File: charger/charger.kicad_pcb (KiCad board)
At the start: 2 copper layers, 42.7 x 32.5 mm, 13 parts, among them J1 USB4515-GF-A_REVA, J2 Screw_Terminal_2_P5.00mm

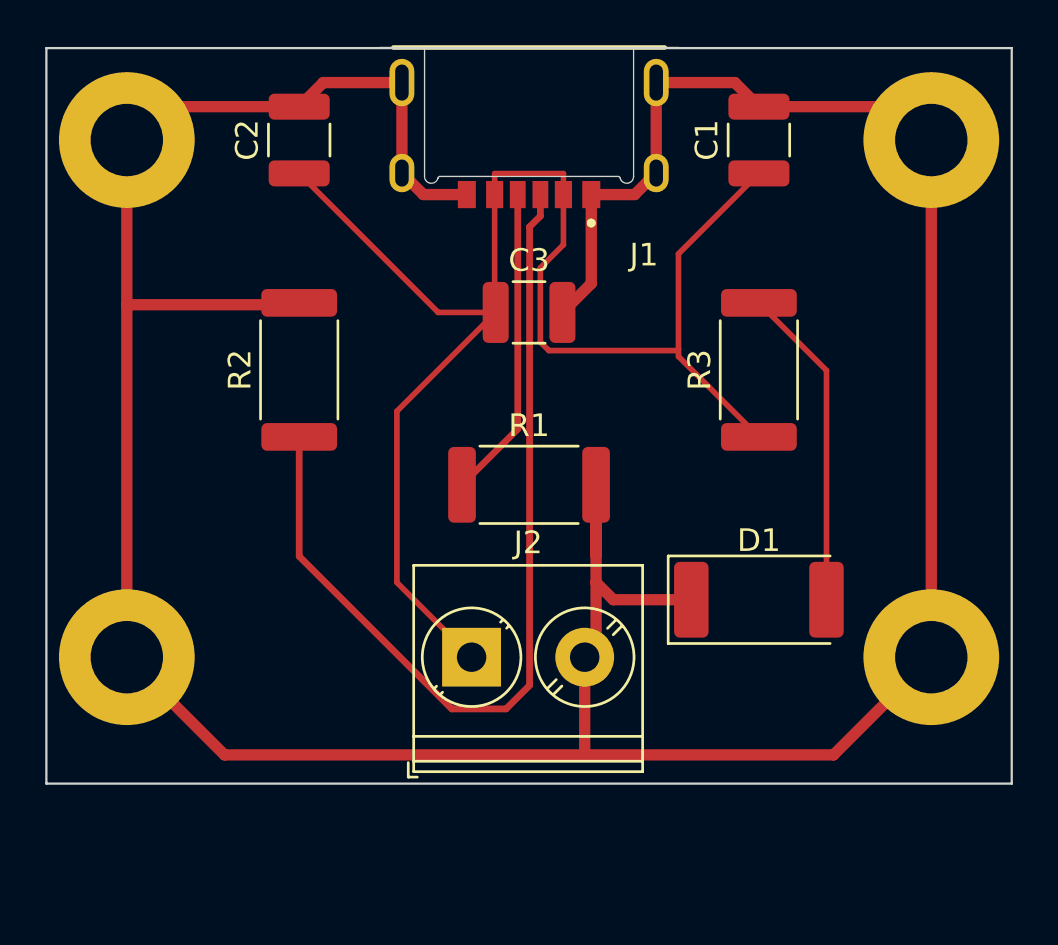
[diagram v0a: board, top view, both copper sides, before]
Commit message: added power/ground planes
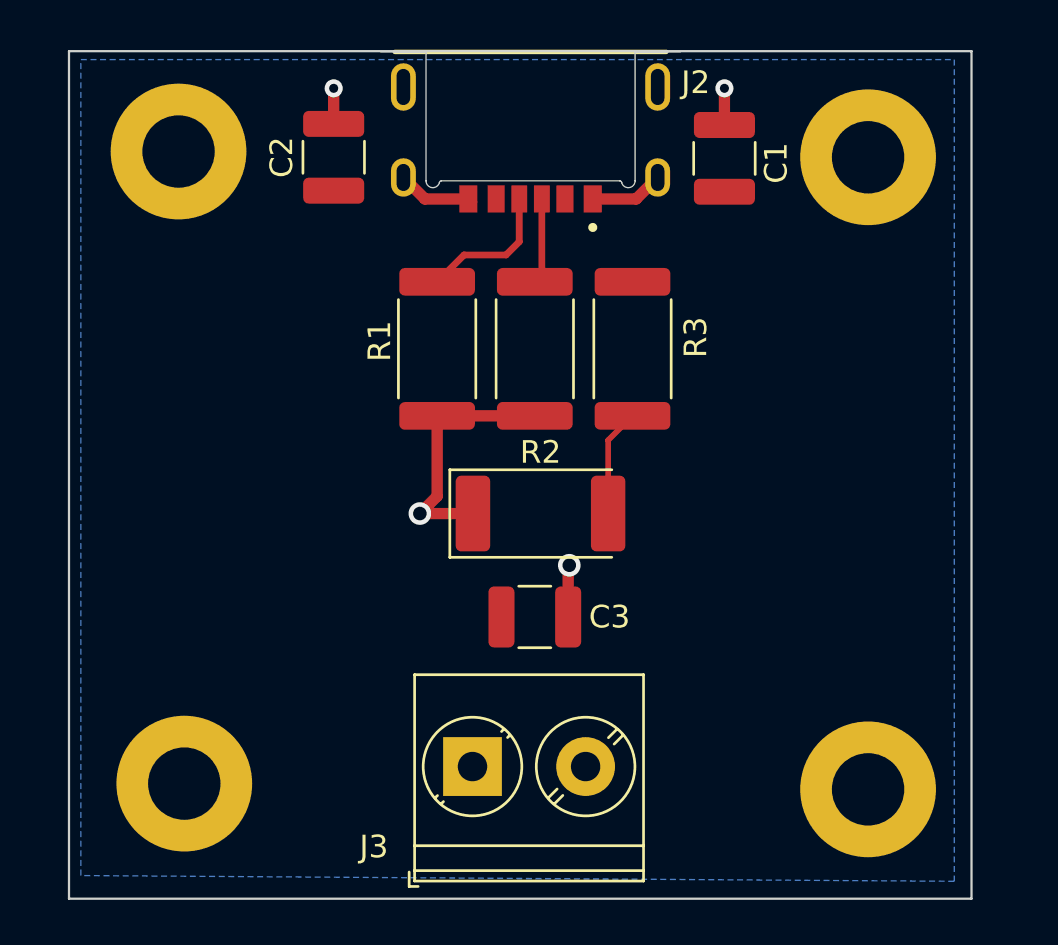
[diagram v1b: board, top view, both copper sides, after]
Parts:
- removed J1: USB4515-GF-A_REVA, USB4515-GF-A_REVA:GCT_USB4515-GF-A_REVA
- added J3: Screw_Terminal_2_P5.00mm, TerminalBlock_Phoenix:TerminalBlock_Phoenix_PT-1,5-2-5.0-H_1x02_P5.00mm_Horizontal, F.Cu at (99.1, 78.5)
- J2: value Screw_Terminal_2_P5.00mm -> USB4515-GF-A_REVA; footprint TerminalBlock_Phoenix:TerminalBlock_Phoenix_PT-1,5-2-5.0-H_1x02_P5.00mm_Horizontal -> USB4515-GF-A_REVA:GCT_USB4515-GF-A_REVA
- moved J2 25.3 mm to (101.7, 48.5), turned to 180 degrees
- moved C3 13.5 mm to (101.9, 71.9)
- moved R2 10.5 mm to (101.9, 60.0), turned to -90 degrees
- moved D1 10.4 mm to (102.1, 67.3)
- moved R1 7.26 mm to (97.5, 60.0), turned to -90 degrees
- moved H4 6.48 mm to (116.6, 79.5)
- moved H3 6.14 mm to (86.4, 79.2)
- moved R3 5.66 mm to (106.2, 60.0), turned to -90 degrees
- moved H2 2.90 mm to (116.6, 51.6)
- moved H1 2.34 mm to (86.1, 51.3)
- moved C1 1.73 mm to (110.2, 51.6)
- moved C2 1.70 mm to (93.0, 51.6)
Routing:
- net GND: track 159.0 -> 23.5 mm, vias 0 -> 4
- net +5V: track 67.6 -> 0.00 mm
- net /CC1: track 40.6 -> 3.79 mm
- net /LED: track 14.4 -> 4.76 mm
- net /CC2: track 13.9 -> 6.26 mm
- added copper zone on B.Cu, net GND
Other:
- board size 42.7 x 32.5 mm -> 39.9 x 37.5 mm

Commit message: fixed segments edge.cuts error and changed the pcb a little bit
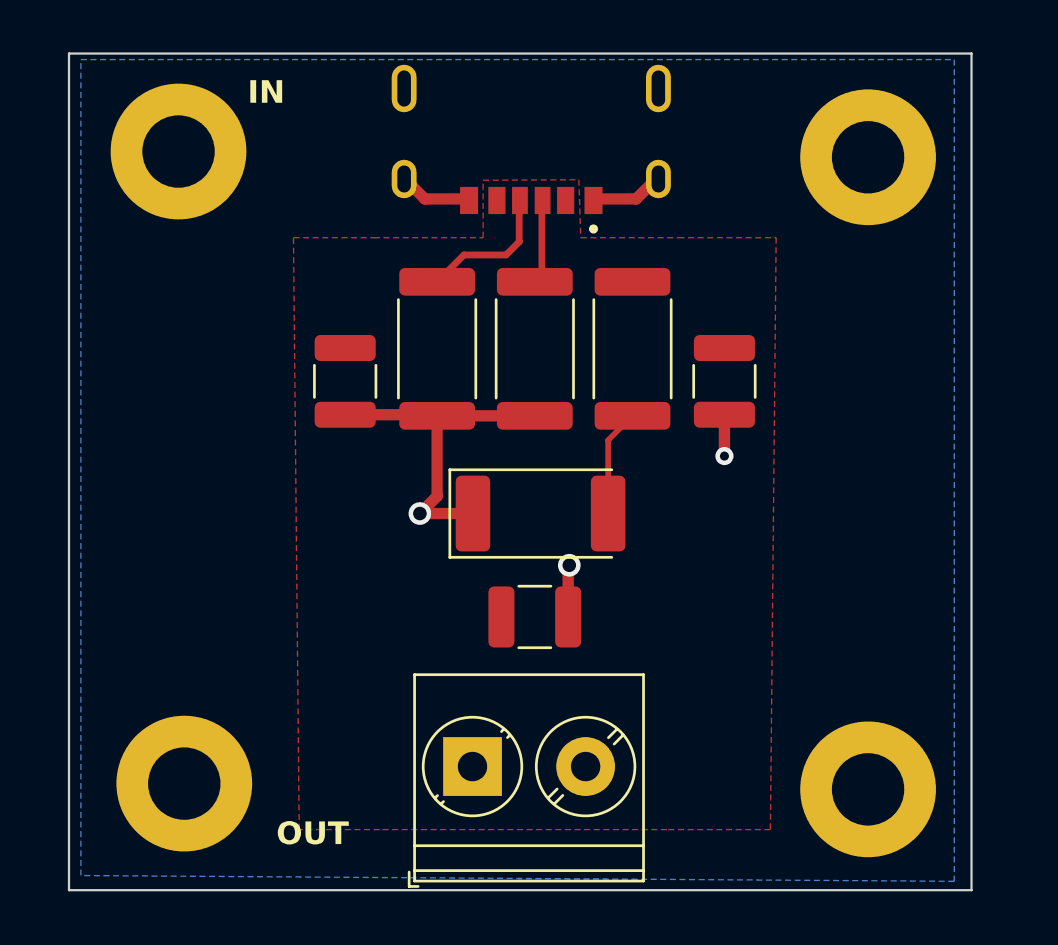
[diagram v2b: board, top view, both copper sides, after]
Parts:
- J2: footprint USB4515-GF-A_REVA:GCT_USB4515-GF-A_REVA -> connectors:USBC_PD_6PINS
- moved C2 9.92 mm to (93.5, 61.5), turned to -90 degrees
- moved C1 9.86 mm to (110.2, 61.5), turned to -90 degrees
- moved J2 0.97 mm to (101.6, 49.4)
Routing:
- net GND: track 23.5 -> 26.2 mm, vias 4 -> 3
- added copper zone on F.Cu, net +5V
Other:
- board size 39.9 x 37.5 mm -> 39.9 x 37 mm
- board text added: "IN"
- board text added: "OUT"

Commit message: ready for testing
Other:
- board text added: "+"
- board text added: "-"
- board text added: "DZ"
- board text added: "Power LED"
- board text added: "PowerS V1.0"
- board text added: "electronics"
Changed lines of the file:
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@@
+	)
+	(gr_rect
+		(start 113.538 58.166)
+		(end 119.888 72.136)
+		(stroke
+			(width 0.2)
+			(type dash_dot)
+		)
+		(fill none)
+		(layer "F.SilkS")
 	)
 	(gr_rect
@@
 		(layer "Edge.Cuts")
 	)
-	(gr_text "IN"
-		(at 89.154 49.276 0)
+	(gr_text "PowerS\nV1.0"
+		(at 86.36 63.5 0)
+		(layer "B.SilkS")
+		(effects
+			(font
+				(size 1.5 1.5)
+				(thickness 0.3)
+				(bold yes)
+			)
+			(justify mirror)
+		)
+	)
+	(gr_text "-"
+		(at 97.536 72.898 0)
 		(layer "F.SilkS")
 		(effects
 			(font
-				(size 1 1)
-				(thickness 0.2)
+				(size 2 2)
+				(thickness 0.35)
 				(bold yes)
 			)
-			(justify left bottom)
+		)
+	)
+	(gr_text "IN"
+		(at 91.948 49.276 0)
+		(layer "F.SilkS")
+		(effects
+			(font
+				(size 2 2)
+				(thickness 0.3)
+			)
+		)
+	)
+	(gr_text "Power \nLED"
+		(at 93.218 67.818 90)
+		(layer "F.SilkS")
+		(effects
+			(font
+				(size 1.7 1.7)
+				(thickness 0.34)
+				(bold yes)
+			)
 		)
 	)
 	(gr_text "OUT"
-		(at 90.424 82.042 0)
+		(at 92.456 80.772 0)
 		(layer "F.SilkS")
 		(effects
 			(font
-				(size 1 1)
-				(thickness 0.2)
+				(size 2 2)
+				(thickness 0.3)
+			)
+		)
+	)
+	(gr_text "electronics"
+		(at 115.57 65.024 -90)
+		(layer "F.SilkS")
+		(effects
+			(font
+				(size 1.5 1.5)
+				(thickness 0.3)
 				(bold yes)
 			)
-			(justify left bottom)
 		)
 	)
+	(gr_text "DZ"
+		(at 117.856 64.262 -90)
+		(layer "F.SilkS")
+		(effects
+			(font
+				(size 2 2)
+				(thickness 0.35)
+				(bold yes)
+			)
+		)
+	)
+	(gr_text "+"
+		(at 105.41 72.644 0)
+		(layer "F.SilkS")
+		(effects
+			(font
+				(size 2 2)
+				(thickness 0.35)
+				(bold yes)
+			)
+		)
+	)
